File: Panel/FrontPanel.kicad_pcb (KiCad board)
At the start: 2 copper layers, 0 parts

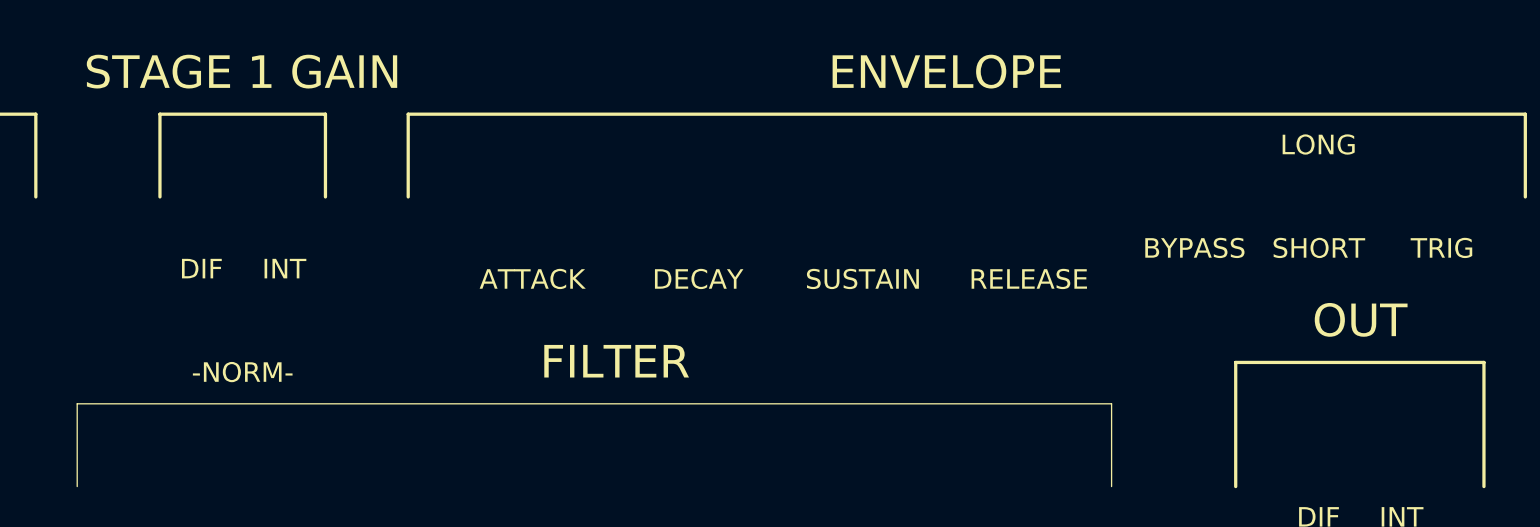
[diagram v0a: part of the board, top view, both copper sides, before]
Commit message: Exported DXFs, added more screw holes
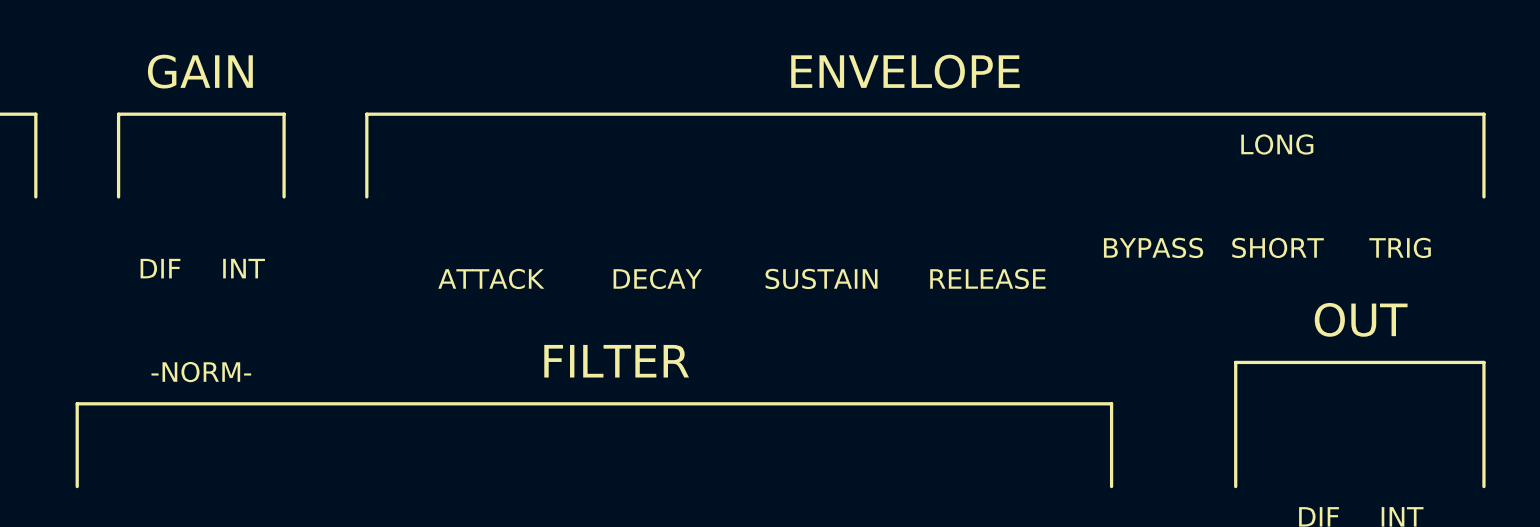
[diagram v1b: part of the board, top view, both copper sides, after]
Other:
- board text removed: "STAGE 1 GAIN"

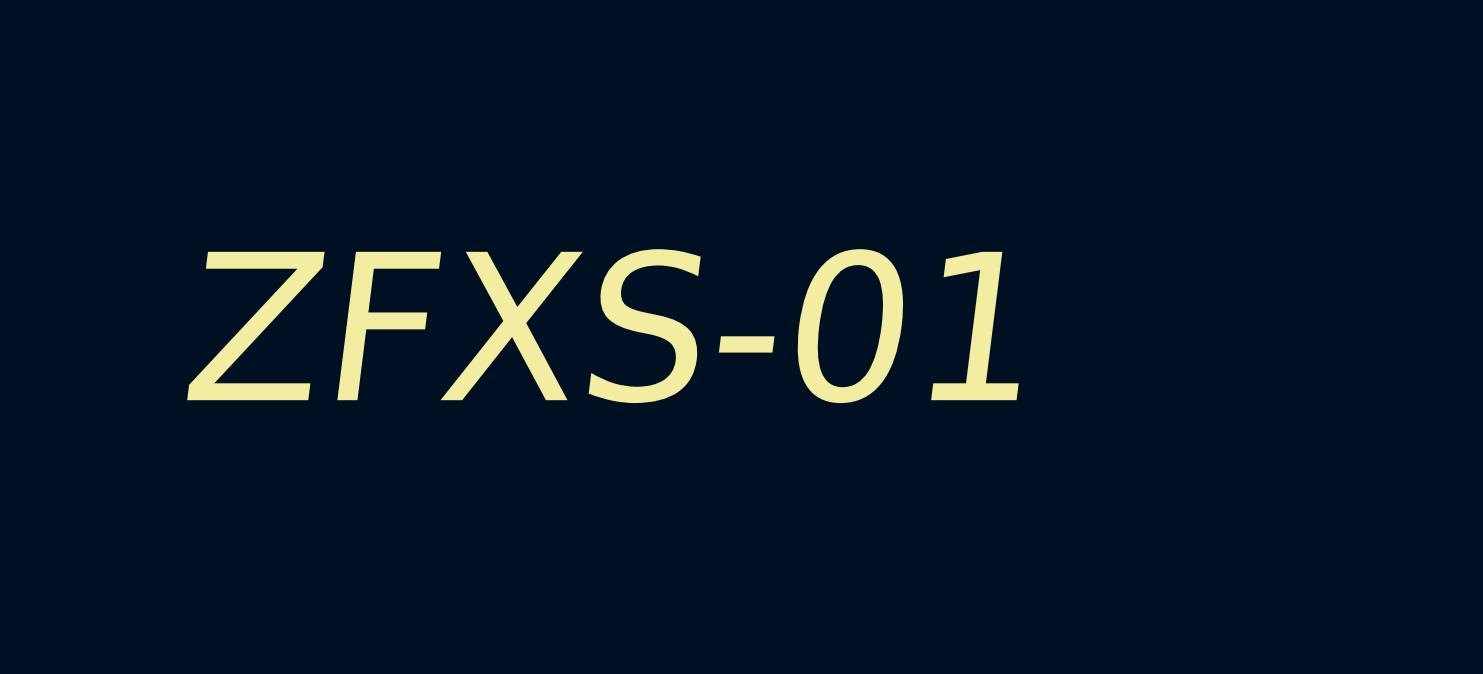
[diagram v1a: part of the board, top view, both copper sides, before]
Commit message: Exported panel, fixed missing net on filter
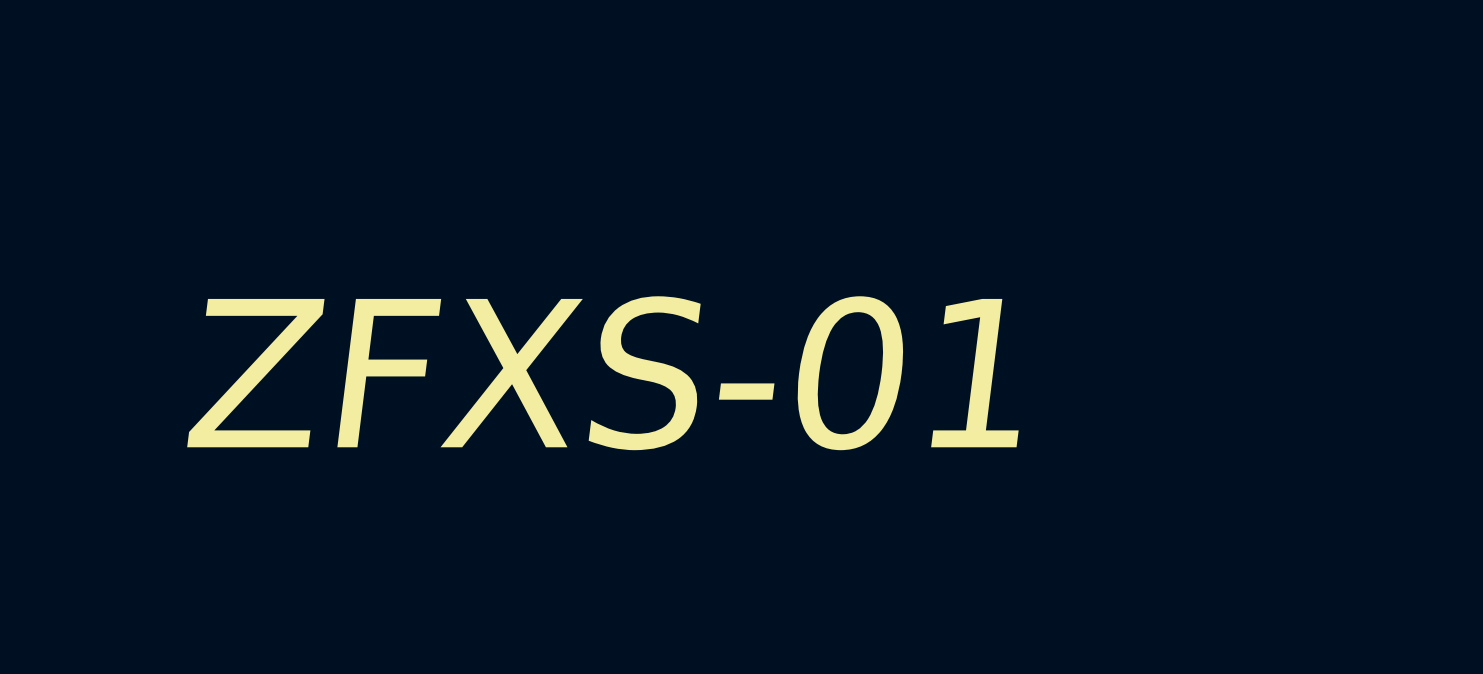
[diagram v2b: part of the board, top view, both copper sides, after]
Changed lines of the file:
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@@
   (general
     (thickness 1.6)
-    (drawings 247)
+    (drawings 249)
     (tracks 0)
     (zones 0)
@@
       (padsonsilk false)
       (subtractmaskfromsilk false)
-      (outputformat 3)
+      (outputformat 5)
       (mirror false)
       (drillshape 0)
       (scaleselection 1)
-      (outputdirectory "dxf/"))
+      (outputdirectory "svg/"))
   )
   (net 0 "")
@@
     (uvia_drill 0.1)
   )
+  (dimension 165.1 (width 0.15) (layer Dwgs.User)
+    (gr_text "165.100 mm" (at -13.999999 133.35 270) (layer Dwgs.User)
+      (effects (font (size 1 1) (thickness 0.15)))
+    )
+    (feature1 (pts (xy 19.05 215.9) (xy -13.28642 215.9)))
+    (feature2 (pts (xy 19.05 50.8) (xy -13.28642 50.8)))
+    (crossbar (pts (xy -12.699999 50.8) (xy -12.699999 215.9)))
+    (arrow1a (pts (xy -12.699999 215.9) (xy -13.28642 214.773496)))
+    (arrow1b (pts (xy -12.699999 215.9) (xy -12.113578 214.773496)))
+    (arrow2a (pts (xy -12.699999 50.8) (xy -13.28642 51.926504)))
+    (arrow2b (pts (xy -12.699999 50.8) (xy -12.113578 51.926504)))
+  )
+  (dimension 520.7 (width 0.15) (layer Dwgs.User)
+    (gr_text "520.700 mm" (at 279.4 11.4) (layer Dwgs.User)
+      (effects (font (size 1 1) (thickness 0.15)))
+    )
+    (feature1 (pts (xy 539.75 50.8) (xy 539.75 12.113579)))
+    (feature2 (pts (xy 19.05 50.8) (xy 19.05 12.113579)))
+    (crossbar (pts (xy 19.05 12.7) (xy 539.75 12.7)))
+    (arrow1a (pts (xy 539.75 12.7) (xy 538.623496 13.286421)))
+    (arrow1b (pts (xy 539.75 12.7) (xy 538.623496 12.113579)))
+    (arrow2a (pts (xy 19.05 12.7) (xy 20.176504 13.286421)))
+    (arrow2b (pts (xy 19.05 12.7) (xy 20.176504 12.113579)))
+  )
   (gr_line (start 304.8 127) (end 304.8 114.3) (layer F.SilkS) (width 0.5))
   (gr_circle (center 304.8 63.5) (end 306.8 63.5) (layer F.Mask) (width 0.15))
-  (gr_circle (center 304.8 201.7) (end 306.8 201.7) (layer F.Mask) (width 0.15))
+  (gr_circle (center 304.8 203.2) (end 306.8 203.2) (layer F.Mask) (width 0.15))
   (gr_circle (center 190.5 203.2) (end 192.5 203.2) (layer F.Mask) (width 0.15))
   (gr_circle (center 190.5 63.5) (end 192.5 63.5) (layer F.Mask) (width 0.15))
@@
     (effects (font (size 3 3) (thickness 0.5)))
   )
-  (gr_text ZFXS-01 (at 44.45 201.6125) (layer F.SilkS)
+  (gr_text ZFXS-01 (at 44.45 203.2) (layer F.SilkS)
     (effects (font (size 5 5) (thickness 1) italic) (justify left))
   )
@@
   (gr_circle (center 209.55 95.25) (end 213.05 95.25) (layer F.Mask) (width 0.15))
   (gr_circle (center 527.05 63.5) (end 529.05 63.5) (layer F.Mask) (width 0.15))
-  (gr_circle (center 31.75 201.7) (end 33.75 201.7) (layer F.Mask) (width 0.15))
+  (gr_circle (center 31.75 203.2) (end 33.75 203.2) (layer F.Mask) (width 0.15))
   (gr_circle (center 31.75 63.5) (end 33.75 63.5) (layer F.Mask) (width 0.15))
-  (gr_circle (center 133.35 165.1) (end 137.1 165.1) (layer F.Mask) (width 0.15))
-  (gr_circle (center 133.35 81.1) (end 134.85 81.1) (layer F.Mask) (width 0.15))
-  (gr_circle (center 171.45 88.9) (end 175.2 88.9) (layer F.Mask) (width 0.15))
-  (gr_circle (center 133.35 127) (end 137.1 127) (layer F.Mask) (width 0.15))
-  (gr_circle (center 133.35 157.3) (end 134.85 157.3) (layer F.Mask) (width 0.15))
-  (gr_circle (center 133.35 119.2) (end 134.85 119.2) (layer F.Mask) (width 0.15))
-  (gr_circle (center 133.35 88.9) (end 137.1 88.9) (layer F.Mask) (width 0.15))
+  (gr_circle (center 133.35 165.1) (end 129.6 165.1) (layer F.Mask) (width 0.15))
+  (gr_circle (center 133.35 96.7) (end 131.85 96.7) (layer F.Mask) (width 0.15))
+  (gr_circle (center 171.45 88.9) (end 167.7 88.9) (layer F.Mask) (width 0.15))
+  (gr_circle (center 133.35 127) (end 129.6 127) (layer F.Mask) (width 0.15))
+  (gr_circle (center 133.35 172.9) (end 131.85 172.9) (layer F.Mask) (width 0.15))
+  (gr_circle (center 133.35 134.8) (end 131.85 134.8) (layer F.Mask) (width 0.15))
+  (gr_circle (center 133.35 88.9) (end 129.6 88.9) (layer F.Mask) (width 0.15))
   (gr_circle (center 158.75 152.4) (end 161.925 152.4) (layer F.Mask) (width 0.15))
   (gr_circle (center 120.65 114.3) (end 123.825 114.3) (layer F.Mask) (width 0.15))
   (gr_circle (center 120.65 76.2) (end 123.825 76.2) (layer F.Mask) (width 0.15))
   (gr_circle (center 120.65 152.4) (end 123.825 152.4) (layer F.Mask) (width 0.15))
-  (gr_circle (center 171.45 119.2) (end 172.95 119.2) (layer F.Mask) (width 0.15))
+  (gr_circle (center 171.45 134.8) (end 169.95 134.8) (layer F.Mask) (width 0.15))
   (gr_circle (center 158.75 114.3) (end 161.925 114.3) (layer F.Mask) (width 0.15))
   (gr_circle (center 158.75 76.2) (end 161.925 76.2) (layer F.Mask) (width 0.15))
-  (gr_circle (center 171.45 81.1) (end 172.95 81.1) (layer F.Mask) (width 0.15))
-  (gr_circle (center 171.45 165.1) (end 175.2 165.1) (layer F.Mask) (width 0.15))
-  (gr_circle (center 171.45 127) (end 175.2 127) (layer F.Mask) (width 0.15))
-  (gr_circle (center 171.45 157.3) (end 172.95 157.3) (layer F.Mask) (width 0.15))
-  (gr_circle (center 95.25 165.1) (end 99 165.1) (layer F.Mask) (width 0.15))
-  (gr_circle (center 95.25 81.1) (end 96.75 81.1) (layer F.Mask) (width 0.15))
-  (gr_circle (center 95.25 127) (end 99 127) (layer F.Mask) (width 0.15))
-  (gr_circle (center 95.25 157.3) (end 96.75 157.3) (layer F.Mask) (width 0.15))
-  (gr_circle (center 95.25 119.2) (end 96.75 119.2) (layer F.Mask) (width 0.15))
-  (gr_circle (center 95.25 88.9) (end 99 88.9) (layer F.Mask) (width 0.15))
+  (gr_circle (center 171.45 96.7) (end 169.95 96.7) (layer F.Mask) (width 0.15))
+  (gr_circle (center 171.45 165.1) (end 167.7 165.1) (layer F.Mask) (width 0.15))
+  (gr_circle (center 171.45 127) (end 167.7 127) (layer F.Mask) (width 0.15))
+  (gr_circle (center 171.45 172.9) (end 169.95 172.9) (layer F.Mask) (width 0.15))
+  (gr_circle (center 95.25 165.1) (end 91.5 165.1) (layer F.Mask) (width 0.15))
+  (gr_circle (center 95.25 96.7) (end 93.75 96.7) (layer F.Mask) (width 0.15))
+  (gr_circle (center 95.25 127) (end 91.5 127) (layer F.Mask) (width 0.15))
+  (gr_circle (center 95.25 172.9) (end 93.75 172.9) (layer F.Mask) (width 0.15))
+  (gr_circle (center 95.25 134.8) (end 93.75 134.8) (layer F.Mask) (width 0.15))
+  (gr_circle (center 95.25 88.9) (end 91.5 88.9) (layer F.Mask) (width 0.15))
   (gr_circle (center 82.55 114.3) (end 85.725 114.3) (layer F.Mask) (width 0.15))
   (gr_circle (center 82.55 76.2) (end 85.725 76.2) (layer F.Mask) (width 0.15))
   (gr_circle (center 82.55 152.4) (end 85.725 152.4) (layer F.Mask) (width 0.15))
-  (gr_circle (center 57.15 157.3) (end 58.65 157.3) (layer F.Mask) (width 0.15))
-  (gr_circle (center 57.15 165.1) (end 60.9 165.1) (layer F.Mask) (width 0.15))
+  (gr_circle (center 57.15 172.9) (end 55.65 172.9) (layer F.Mask) (width 0.15))
+  (gr_circle (center 57.15 165.1) (end 53.4 165.1) (layer F.Mask) (width 0.15))
   (gr_circle (center 44.45 152.4) (end 47.625 152.4) (layer F.Mask) (width 0.15))
-  (gr_circle (center 57.15 119.2) (end 58.65 119.2) (layer F.Mask) (width 0.15))
-  (gr_circle (center 57.15 127) (end 60.9 127) (layer F.Mask) (width 0.15))
+  (gr_circle (center 57.15 134.8) (end 55.65 134.8) (layer F.Mask) (width 0.15))
+  (gr_circle (center 57.15 127) (end 53.4 127) (layer F.Mask) (width 0.15))
   (gr_circle (center 44.45 114.3) (end 47.625 114.3) (layer F.Mask) (width 0.15))
   (gr_circle (center 44.45 76.2) (end 47.625 76.2) (layer F.Mask) (width 0.15))
-  (gr_circle (center 57.15 81.1) (end 58.65 81.1) (layer F.Mask) (width 0.15))
-  (gr_circle (center 57.15 88.9) (end 60.9 88.9) (layer F.Mask) (width 0.15))
+  (gr_circle (center 57.15 96.7) (end 55.65 96.7) (layer F.Mask) (width 0.15))
+  (gr_circle (center 57.15 88.9) (end 53.4 88.9) (layer F.Mask) (width 0.15))
   (gr_line (start 19.05 215.9) (end 19.05 50.8) (layer F.Mask) (width 0.15))
   (gr_line (start 539.75 215.9) (end 19.05 215.9) (layer F.Mask) (width 0.15))
